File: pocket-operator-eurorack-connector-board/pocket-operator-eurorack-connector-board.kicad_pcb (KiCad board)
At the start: 2 copper layers, 6 parts, among them J1 Conn_02x04_Odd_Even, J2 AudioJack2_SwitchT, J3 AudioJack2_SwitchT, J4 AudioJack2_SwitchT, J5 AudioJack2_SwitchT, SW1 SW_Push_SPDT

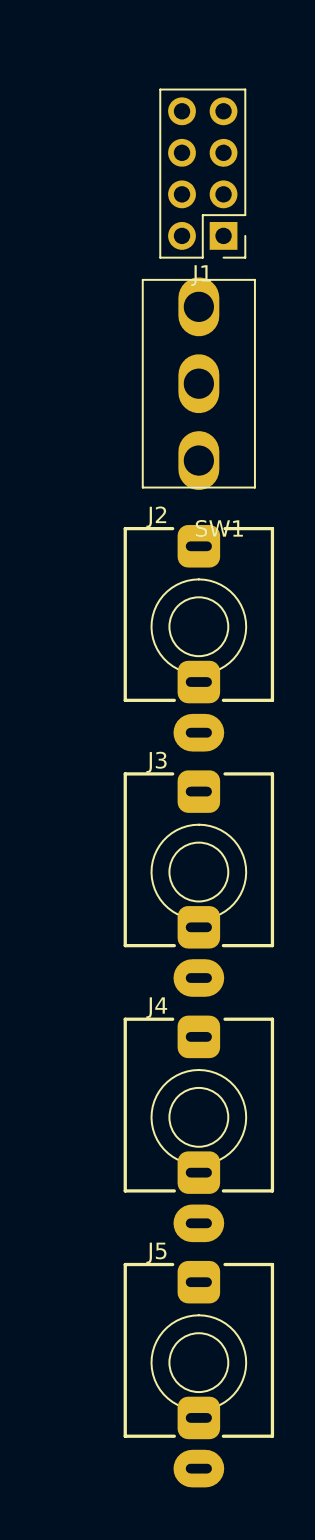
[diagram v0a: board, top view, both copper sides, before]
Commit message: connector board placed and tracked
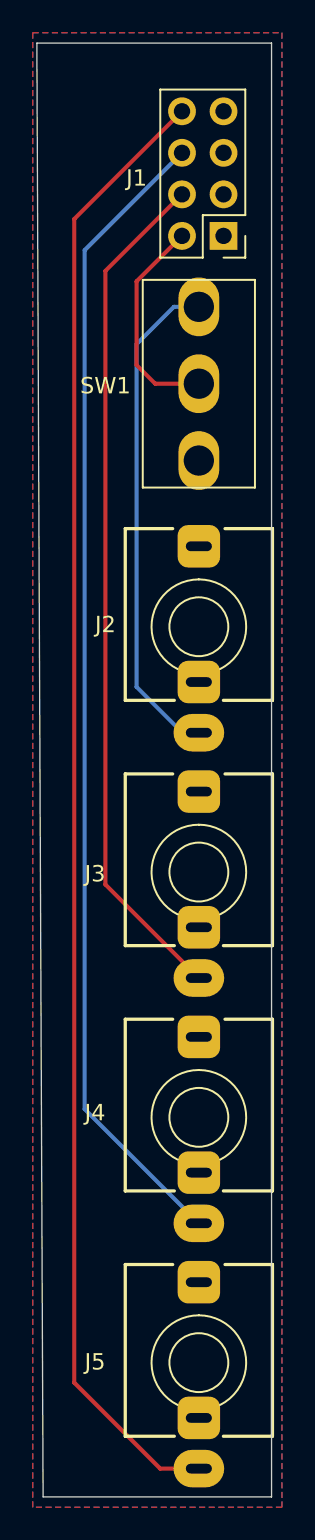
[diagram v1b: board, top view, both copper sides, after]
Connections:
- J1 pad 1: /IN_L -> GND
- J1 pad 2: GND -> /IN_L
- J1 pad 3: /IN_R -> GND
- J1 pad 4: GND -> /IN_R
- J1 pad 5: /OUT_L -> GND
- J1 pad 6: GND -> /OUT_L
- J1 pad 7: /OUT_R -> GND
- J1 pad 8: GND -> /OUT_R
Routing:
- net /OUT_R: track 0.00 -> 90.3 mm
- net /OUT_L: track 0.00 -> 70.8 mm
- net /IN_R: track 0.00 -> 52.2 mm
- net Net-(J2-PadS): track 0.00 -> 30.7 mm
- net /IN_L: track 0.00 -> 13.3 mm
- added copper zone on B.Cu, net GND
- added copper zone on F.Cu, net GND
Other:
- board outline added: 14.4 x 88.9 mm
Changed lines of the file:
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@@
   (general
     (thickness 1.6)
-    (drawings 0)
-    (tracks 0)
+    (drawings 4)
+    (tracks 19)
     (zones 0)
     (modules 6)
@@
     (46 B.CrtYd user)
     (47 F.CrtYd user)
-    (48 B.Fab user)
-    (49 F.Fab user)
+    (48 B.Fab user hide)
+    (49 F.Fab user hide)
   )
   (setup
@@
     (descr "Through hole straight pin header, 2x04, 2.54mm pitch, double rows")
     (tags "Through hole pin header THT 2x04 2.54mm double row")
-    (fp_text reference J1 (at 1.27 -2.33) (layer F.SilkS)
+    (fp_text reference J1 (at 5.32 3.535) (layer F.SilkS)
       (effects (font (size 1 1) (thickness 0.15)))
     )
@@
     )
     (pad 1 thru_hole rect (at 0 0 180) (size 1.7 1.7) (drill 1) (layers *.Cu *.Mask)
+      (net 2 GND))
+    (pad 2 thru_hole oval (at 2.54 0 180) (size 1.7 1.7) (drill 1) (layers *.Cu *.Mask)
       (net 1 /IN_L))
-    (pad 2 thru_hole oval (at 2.54 0 180) (size 1.7 1.7) (drill 1) (layers *.Cu *.Mask)
-      (net 2 GND))
     (pad 3 thru_hole oval (at 0 2.54 180) (size 1.7 1.7) (drill 1) (layers *.Cu *.Mask)
+      (net 2 GND))
+    (pad 4 thru_hole oval (at 2.54 2.54 180) (size 1.7 1.7) (drill 1) (layers *.Cu *.Mask)
       (net 3 /IN_R))
-    (pad 4 thru_hole oval (at 2.54 2.54 180) (size 1.7 1.7) (drill 1) (layers *.Cu *.Mask)
-      (net 2 GND))
     (pad 5 thru_hole oval (at 0 5.08 180) (size 1.7 1.7) (drill 1) (layers *.Cu *.Mask)
+      (net 2 GND))
+    (pad 6 thru_hole oval (at 2.54 5.08 180) (size 1.7 1.7) (drill 1) (layers *.Cu *.Mask)
       (net 4 /OUT_L))
-    (pad 6 thru_hole oval (at 2.54 5.08 180) (size 1.7 1.7) (drill 1) (layers *.Cu *.Mask)
-      (net 2 GND))
     (pad 7 thru_hole oval (at 0 7.62 180) (size 1.7 1.7) (drill 1) (layers *.Cu *.Mask)
+      (net 2 GND))
+    (pad 8 thru_hole oval (at 2.54 7.62 180) (size 1.7 1.7) (drill 1) (layers *.Cu *.Mask)
       (net 5 /OUT_R))
-    (pad 8 thru_hole oval (at 2.54 7.62 180) (size 1.7 1.7) (drill 1) (layers *.Cu *.Mask)
-      (net 2 GND))
     (model ${KISYS3DMOD}/Connector_PinHeader_2.54mm.3dshapes/PinHeader_2x04_P2.54mm_Vertical.wrl
       (at (xyz 0 0 0))
@@
     (descr "T-S-SN Vertical mount jack AKA WQP-WQP518MA or Thonkiconn")
     (tags "WQP-WQP518MA, Thonkiconn")
-    (fp_text reference J2 (at -2.5 -6.8) (layer F.SilkS)
+    (fp_text reference J2 (at -5.715 -0.13) (layer F.SilkS)
       (effects (font (size 1 1) (thickness 0.15)))
     )
@@
     (descr "T-S-SN Vertical mount jack AKA WQP-WQP518MA or Thonkiconn")
     (tags "WQP-WQP518MA, Thonkiconn")
-    (fp_text reference J3 (at -2.5 -6.8) (layer F.SilkS)
+    (fp_text reference J3 (at -6.35 0.11) (layer F.SilkS)
       (effects (font (size 1 1) (thickness 0.15)))
     )
@@
     (descr "T-S-SN Vertical mount jack AKA WQP-WQP518MA or Thonkiconn")
     (tags "WQP-WQP518MA, Thonkiconn")
-    (fp_text reference J4 (at -2.5 -6.8) (layer F.SilkS)
+    (fp_text reference J4 (at -6.35 -0.285) (layer F.SilkS)
       (effects (font (size 1 1) (thickness 0.15)))
     )
@@
     (descr "T-S-SN Vertical mount jack AKA WQP-WQP518MA or Thonkiconn")
     (tags "WQP-WQP518MA, Thonkiconn")
-    (fp_text reference J5 (at -2.5 -6.8) (layer F.SilkS)
+    (fp_text reference J5 (at -6.35 -0.045) (layer F.SilkS)
       (effects (font (size 1 1) (thickness 0.15)))
     )
@@
   (module mylibs:SW_6mm_SPDT (layer F.Cu)
     (at 0 24.638)
-    (fp_text reference SW1 (at 1.27 8.89) (layer F.SilkS)
+    (fp_text reference SW1 (at -5.715 0.127) (layer F.SilkS)
       (effects (font (size 1 1) (thickness 0.15)))
     )
@@
       (net 11 "Net-(SW1-Pad3)"))
   )
+  (gr_line (start -9.525 92.71) (end -9.906 3.81) (layer Edge.Cuts) (width 0.05))
+  (gr_line (start 4.445 92.71) (end -9.525 92.71) (layer Edge.Cuts) (width 0.05))
+  (gr_line (start 4.445 3.81) (end 4.445 92.71) (layer Edge.Cuts) (width 0.05))
+  (gr_line (start -9.906 3.81) (end 4.445 3.81) (layer Edge.Cuts) (width 0.05))
+  (segment (start -1.03 15.6) (end -3.81 18.38) (width 0.25) (layer F.Cu) (net 1))
+  (segment (start -3.81 18.38) (end -3.81 23.495) (width 0.25) (layer F.Cu) (net 1))
+  (segment (start -2.667 24.638) (end 0 24.638) (width 0.25) (layer F.Cu) (net 1))
+  (segment (start -3.81 23.495) (end -2.667 24.638) (width 0.25) (layer F.Cu) (net 1))
+  (segment (start -1.03 13.06) (end -5.715 17.745) (width 0.25) (layer F.Cu) (net 3))
+  (segment (start -5.715 55.265) (end 0 60.98) (width 0.25) (layer F.Cu) (net 3))
+  (segment (start -5.715 17.745) (end -5.715 55.265) (width 0.25) (layer F.Cu) (net 3))
+  (segment (start -1.03 10.52) (end -6.985 16.475) (width 0.25) (layer B.Cu) (net 4))
+  (segment (start -6.985 68.995) (end 0 75.98) (width 0.25) (layer B.Cu) (net 4))
+  (segment (start -6.985 16.475) (end -6.985 68.995) (width 0.25) (layer B.Cu) (net 4))
+  (segment (start -1.03 7.98) (end -7.62 14.57) (width 0.25) (layer F.Cu) (net 5))
+  (segment (start -7.62 14.57) (end -7.62 85.725) (width 0.25) (layer F.Cu) (net 5))
+  (segment (start -2.365 90.98) (end 0 90.98) (width 0.25) (layer F.Cu) (net 5))
+  (segment (start -7.62 85.725) (end -2.365 90.98) (width 0.25) (layer F.Cu) (net 5))
+  (segment (start 0 19.938) (end -1.523 19.938) (width 0.25) (layer B.Cu) (net 6))
+  (segment (start -1.523 19.938) (end -3.81 22.225) (width 0.25) (layer B.Cu) (net 6))
+  (segment (start -3.81 22.225) (end -3.81 43.18) (width 0.25) (layer B.Cu) (net 6))
+  (segment (start -1.01 45.98) (end 0 45.98) (width 0.25) (layer B.Cu) (net 6))
+  (segment (start -3.81 43.18) (end -1.01 45.98) (width 0.25) (layer B.Cu) (net 6))
+  (zone (net 2) (net_name GND) (layer F.Cu) (hatch edge 0.508)
+    (connect_pads (clearance 0.508))
+    (min_thickness 0.254)
+    (fill yes (arc_segments 32) (thermal_gap 0.508) (thermal_bridge_width 0.508))
+    (polygon
+      (pts
+        (xy 5.08 93.345) (xy -10.16 93.345) (xy -10.16 3.175) (xy 5.08 3.175)
+      )
+    )
+  )
+  (zone (net 2) (net_name GND) (layer B.Cu) (hatch edge 0.508)
+    (connect_pads (clearance 0.508))
+    (min_thickness 0.254)
+    (fill yes (arc_segments 32) (thermal_gap 0.508) (thermal_bridge_width 0.508))
+    (polygon
+      (pts
+        (xy 5.08 93.345) (xy -10.16 93.345) (xy -10.16 3.175) (xy 5.08 3.175)
+      )
+    )
+  )
 )
